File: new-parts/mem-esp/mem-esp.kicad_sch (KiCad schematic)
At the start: 63 parts, among them J1 Conn_02x02_Odd_Even, J2 BHR-10-VUA, J3 BHR-10-VUA, J4 Conn_02x01, J5 Conn_02x01, J6 Conn_02x01, J7 Conn_02x01, U1 MC78M06_TO252, U2 ESP32-S3-DevKitC, U3 LTV-247, U4 LTV-247, U5 DRV8908, U6 LTV-247, U7 LTV-247, U8 LTV-247

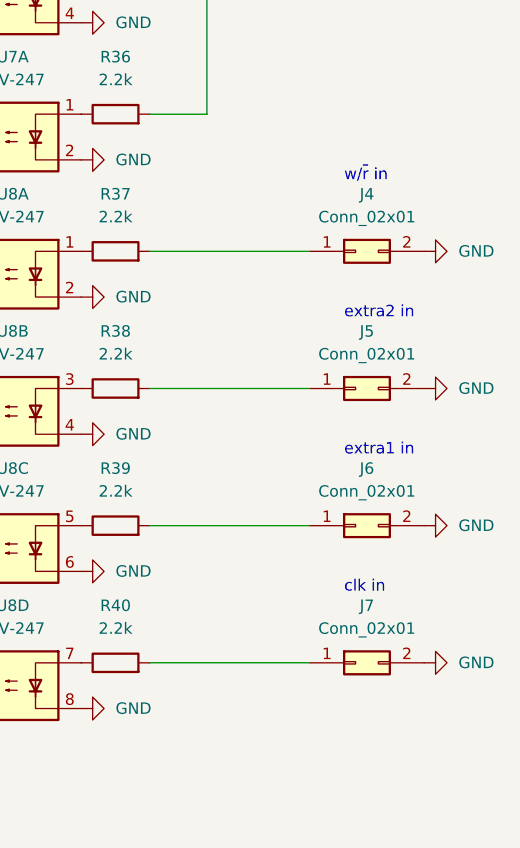
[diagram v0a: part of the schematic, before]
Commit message: Change all two-pin headers for control + ground to control only.
This is to prevent accidental short circuits when they are plugged in the
wrong way.
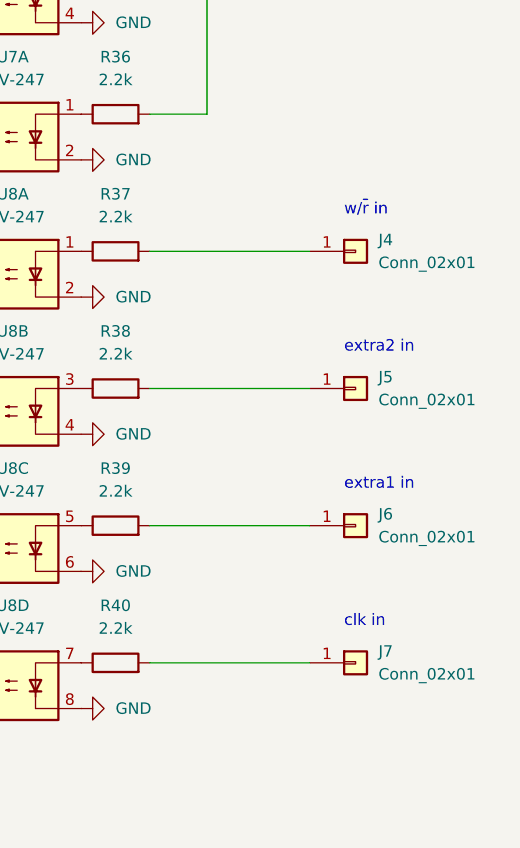
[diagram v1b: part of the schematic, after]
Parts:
- J4, J5, J6, J7: footprint Connector_PinHeader_2.54mm:PinHeader_1x02_P2.54mm_Vertical -> Connector_PinHeader_2.54mm:PinHeader_1x01_P2.54mm_Vertical; symbol Connector_Generic:Conn_02x01 -> Connector_Generic:Conn_01x01
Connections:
- net GND: no longer J4.2 (Pin_2), J5.2 (Pin_2), J6.2 (Pin_2), J7.2 (Pin_2)
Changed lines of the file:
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@@
     (effects (font (size 1.27 1.27)) (justify left top))
   )
-  (text "clk in" (at 386.08 182.88 0)
+  (text "clk in" (at 386.08 186.69 0)
     (effects (font (size 1.27 1.27)) (justify left bottom))
   )
-  (text "w/~{r} in" (at 386.08 137.16 0)
+  (text "w/~{r} in" (at 386.08 140.97 0)
     (effects (font (size 1.27 1.27)) (justify left bottom))
   )
@@
     (effects (font (size 1.27 1.27)) (justify left bottom))
   )
-  (text "extra2 in" (at 386.08 152.4 0)
+  (text "extra2 in" (at 386.08 156.21 0)
     (effects (font (size 1.27 1.27)) (justify left bottom))
   )
-  (text "extra1 in" (at 386.08 167.64 0)
+  (text "extra1 in" (at 386.08 171.45 0)
     (effects (font (size 1.27 1.27)) (justify left bottom))
   )
@@
     )
   )
-  (symbol (lib_id "Connector_Generic:Conn_02x01") (at 387.35 160.02 0) (unit 1)
+  (symbol (lib_id "Connector_Generic:Conn_01x01") (at 387.35 160.02 0) (unit 1)
     (in_bom yes) (on_board yes) (dnp no) (fields_autoplaced)
-    (property "Reference" "J5" (at 388.62 153.67 0)
-      (effects (font (size 1.27 1.27)))
+    (property "Reference" "J5" (at 389.89 158.75 0)
+      (effects (font (size 1.27 1.27)) (justify left))
     )
-    (property "Value" "Conn_02x01" (at 388.62 156.21 0)
-      (effects (font (size 1.27 1.27)))
+    (property "Value" "Conn_02x01" (at 389.89 161.29 0)
+      (effects (font (size 1.27 1.27)) (justify left))
     )
-    (property "Footprint" "Connector_PinHeader_2.54mm:PinHeader_1x02_P2.54mm_Vertical" (at 387.35 160.02 0)
+    (property "Footprint" "Connector_PinHeader_2.54mm:PinHeader_1x01_P2.54mm_Vertical" (at 387.35 160.02 0)
       (effects (font (size 1.27 1.27)) hide)
     )
@@
     )
     (pin "1")
-    (pin "2")
     (instances
       (project "mem-esp"
@@
     )
   )
-  (symbol (lib_id "Connector_Generic:Conn_02x01") (at 387.35 190.5 0) (unit 1)
+  (symbol (lib_id "Connector_Generic:Conn_01x01") (at 387.35 190.5 0) (unit 1)
     (in_bom yes) (on_board yes) (dnp no) (fields_autoplaced)
-    (property "Reference" "J7" (at 388.62 184.15 0)
-      (effects (font (size 1.27 1.27)))
+    (property "Reference" "J7" (at 389.89 189.23 0)
+      (effects (font (size 1.27 1.27)) (justify left))
     )
-    (property "Value" "Conn_02x01" (at 388.62 186.69 0)
-      (effects (font (size 1.27 1.27)))
+    (property "Value" "Conn_02x01" (at 389.89 191.77 0)
+      (effects (font (size 1.27 1.27)) (justify left))
     )
-    (property "Footprint" "Connector_PinHeader_2.54mm:PinHeader_1x02_P2.54mm_Vertical" (at 387.35 190.5 0)
+    (property "Footprint" "Connector_PinHeader_2.54mm:PinHeader_1x01_P2.54mm_Vertical" (at 387.35 190.5 0)
       (effects (font (size 1.27 1.27)) hide)
     )
@@
     )
     (pin "1")
-    (pin "2")
     (instances
       (project "mem-esp"
@@
     )
   )
-  (symbol (lib_id "power:GND") (at 394.97 175.26 90) (unit 1)
-    (in_bom yes) (on_board yes) (dnp no) (fields_autoplaced)
-    (property "Reference" "#PWR094" (at 401.32 175.26 0)
-      (effects (font (size 1.27 1.27)) hide)
-    )
-    (property "Value" "GND" (at 398.78 175.26 90)
-      (effects (font (size 1.27 1.27)) (justify right))
-    )
-    (property "Footprint" "" (at 394.97 175.26 0)
-      (effects (font (size 1.27 1.27)) hide)
-    )
-    (property "Datasheet" "" (at 394.97 175.26 0)
-      (effects (font (size 1.27 1.27)) hide)
-    )
-    (pin "1")
-    (instances
-      (project "mem-esp"
-        (path "/8e7358e7-c3ef-4f3e-9154-e7eba01c544e"
-          (reference "#PWR094") (unit 1)
-        )
-      )
-    )
-  )
   (symbol (lib_id "power:+3V3") (at 231.14 99.06 90) (unit 1)
     (in_bom yes) (on_board yes) (dnp no) (fields_autoplaced)
@@
     )
   )
-  (symbol (lib_id "power:GND") (at 394.97 144.78 90) (unit 1)
-    (in_bom yes) (on_board yes) (dnp no) (fields_autoplaced)
-    (property "Reference" "#PWR093" (at 401.32 144.78 0)
-      (effects (font (size 1.27 1.27)) hide)
-    )
-    (property "Value" "GND" (at 398.78 144.78 90)
-      (effects (font (size 1.27 1.27)) (justify right))
-    )
-    (property "Footprint" "" (at 394.97 144.78 0)
-      (effects (font (size 1.27 1.27)) hide)
-    )
-    (property "Datasheet" "" (at 394.97 144.78 0)
-      (effects (font (size 1.27 1.27)) hide)
-    )
-    (pin "1")
-    (instances
-      (project "mem-esp"
-        (path "/8e7358e7-c3ef-4f3e-9154-e7eba01c544e"
-          (reference "#PWR093") (unit 1)
-        )
-      )
-    )
-  )
   (symbol (lib_id "Isolator:LTV-247") (at 349.25 101.6 0) (mirror y) (unit 3)
     (in_bom yes) (on_board yes) (dnp no) (fields_autoplaced)
@@
     )
   )
-  (symbol (lib_id "Connector_Generic:Conn_02x01") (at 387.35 144.78 0) (unit 1)
+  (symbol (lib_id "Connector_Generic:Conn_01x01") (at 387.35 144.78 0) (unit 1)
     (in_bom yes) (on_board yes) (dnp no) (fields_autoplaced)
-    (property "Reference" "J4" (at 388.62 138.43 0)
-      (effects (font (size 1.27 1.27)))
+    (property "Reference" "J4" (at 389.89 143.51 0)
+      (effects (font (size 1.27 1.27)) (justify left))
     )
-    (property "Value" "Conn_02x01" (at 388.62 140.97 0)
-      (effects (font (size 1.27 1.27)))
+    (property "Value" "Conn_02x01" (at 389.89 146.05 0)
+      (effects (font (size 1.27 1.27)) (justify left))
     )
-    (property "Footprint" "Connector_PinHeader_2.54mm:PinHeader_1x02_P2.54mm_Vertical" (at 387.35 144.78 0)
+    (property "Footprint" "Connector_PinHeader_2.54mm:PinHeader_1x01_P2.54mm_Vertical" (at 387.35 144.78 0)
       (effects (font (size 1.27 1.27)) hide)
     )
@@
     )
     (pin "1")
-    (pin "2")
     (instances
       (project "mem-esp"
@@
     )
   )
-  (symbol (lib_id "power:GND") (at 394.97 160.02 90) (unit 1)
-    (in_bom yes) (on_board yes) (dnp no) (fields_autoplaced)
-    (property "Reference" "#PWR095" (at 401.32 160.02 0)
-      (effects (font (size 1.27 1.27)) hide)
-    )
-    (property "Value" "GND" (at 398.78 160.02 90)
-      (effects (font (size 1.27 1.27)) (justify right))
-    )
-    (property "Footprint" "" (at 394.97 160.02 0)
-      (effects (font (size 1.27 1.27)) hide)
-    )
-    (property "Datasheet" "" (at 394.97 160.02 0)
-      (effects (font (size 1.27 1.27)) hide)
-    )
-    (pin "1")
-    (instances
-      (project "mem-esp"
-        (path "/8e7358e7-c3ef-4f3e-9154-e7eba01c544e"
-          (reference "#PWR095") (unit 1)
-        )
-      )
-    )
-  )
   (symbol (lib_id "power:+3V3") (at 231.14 68.58 90) (unit 1)
     (in_bom yes) (on_board yes) (dnp no) (fields_autoplaced)
@@
     )
   )
-  (symbol (lib_id "Connector_Generic:Conn_02x01") (at 387.35 175.26 0) (unit 1)
+  (symbol (lib_id "Connector_Generic:Conn_01x01") (at 387.35 175.26 0) (unit 1)
     (in_bom yes) (on_board yes) (dnp no) (fields_autoplaced)
-    (property "Reference" "J6" (at 388.62 168.91 0)
-      (effects (font (size 1.27 1.27)))
+    (property "Reference" "J6" (at 389.89 173.99 0)
+      (effects (font (size 1.27 1.27)) (justify left))
     )
-    (property "Value" "Conn_02x01" (at 388.62 171.45 0)
-      (effects (font (size 1.27 1.27)))
+    (property "Value" "Conn_02x01" (at 389.89 176.53 0)
+      (effects (font (size 1.27 1.27)) (justify left))
     )
-    (property "Footprint" "Connector_PinHeader_2.54mm:PinHeader_1x02_P2.54mm_Vertical" (at 387.35 175.26 0)
+    (property "Footprint" "Connector_PinHeader_2.54mm:PinHeader_1x01_P2.54mm_Vertical" (at 387.35 175.26 0)
       (effects (font (size 1.27 1.27)) hide)
     )
@@
     )
     (pin "1")
-    (pin "2")
     (instances
       (project "mem-esp"
@@
         )
       )
-    )
-  )
-  (symbol (lib_id "power:GND") (at 394.97 190.5 90) (unit 1)
-    (in_bom yes) (on_board yes) (dnp no) (fields_autoplaced)
-    (property "Reference" "#PWR092" (at 401.32 190.5 0)
-      (effects (font (size 1.27 1.27)) hide)
-    )
-    (property "Value" "GND" (at 398.78 190.5 90)
-      (effects (font (size 1.27 1.27)) (justify right))
-    )
-    (property "Footprint" "" (at 394.97 190.5 0)
-      (effects (font (size 1.27 1.27)) hide)
-    )
-    (property "Datasheet" "" (at 394.97 190.5 0)
-      (effects (font (size 1.27 1.27)) hide)
-    )
-    (pin "1")
-    (instances
-      (project "mem-esp"
-        (path "/8e7358e7-c3ef-4f3e-9154-e7eba01c544e"
-          (reference "#PWR092") (unit 1)
-        )
-      )

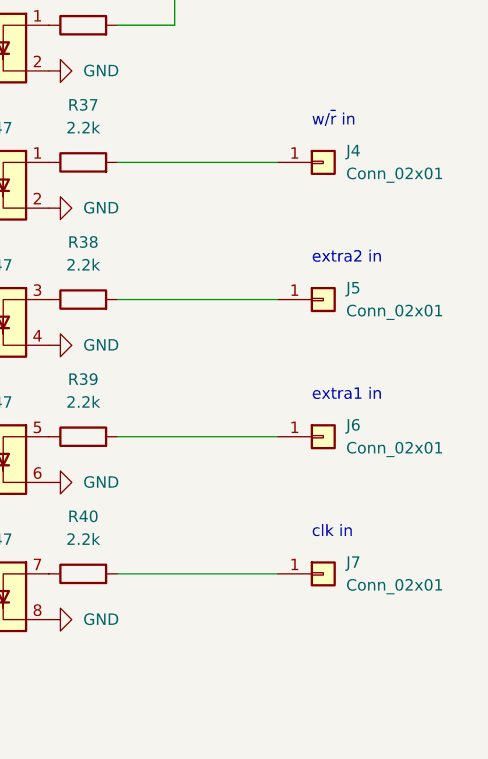
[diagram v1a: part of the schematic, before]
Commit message: Fix connector values: change names from 2 rows to 1 row.
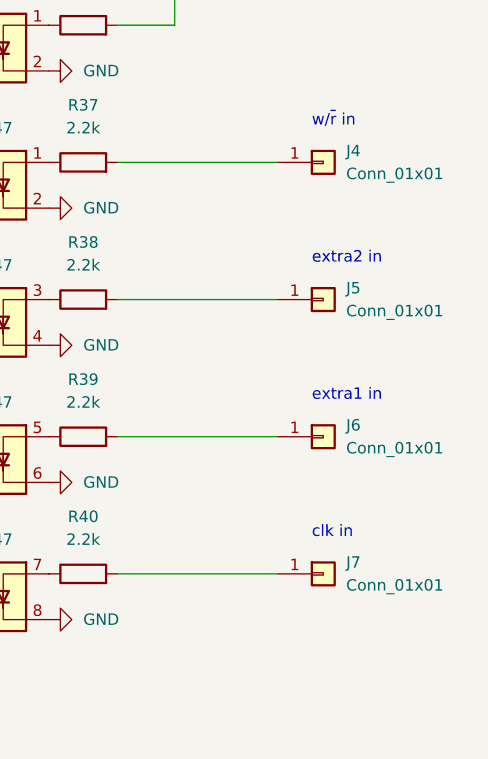
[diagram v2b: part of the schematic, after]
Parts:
- J4, J5, J6, J7: value Conn_02x01 -> Conn_01x01
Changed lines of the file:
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@@
       (effects (font (size 1.27 1.27)) (justify left))
     )
-    (property "Value" "Conn_02x01" (at 389.89 161.29 0)
+    (property "Value" "Conn_01x01" (at 389.89 161.29 0)
       (effects (font (size 1.27 1.27)) (justify left))
     )
@@
       (effects (font (size 1.27 1.27)) (justify left))
     )
-    (property "Value" "Conn_02x01" (at 389.89 191.77 0)
+    (property "Value" "Conn_01x01" (at 389.89 191.77 0)
       (effects (font (size 1.27 1.27)) (justify left))
     )
@@
       (effects (font (size 1.27 1.27)) (justify left))
     )
-    (property "Value" "Conn_02x01" (at 389.89 146.05 0)
+    (property "Value" "Conn_01x01" (at 389.89 146.05 0)
       (effects (font (size 1.27 1.27)) (justify left))
     )
@@
       (effects (font (size 1.27 1.27)) (justify left))
     )
-    (property "Value" "Conn_02x01" (at 389.89 176.53 0)
-      (effects (font (size 1.27 1.27)) (justify left))
-    )
+    (property "Value" "Conn_01x01" (at 389.89 176.53 0)
+      (effects (font (size 1.27 1.27)) (justify left))
+    )

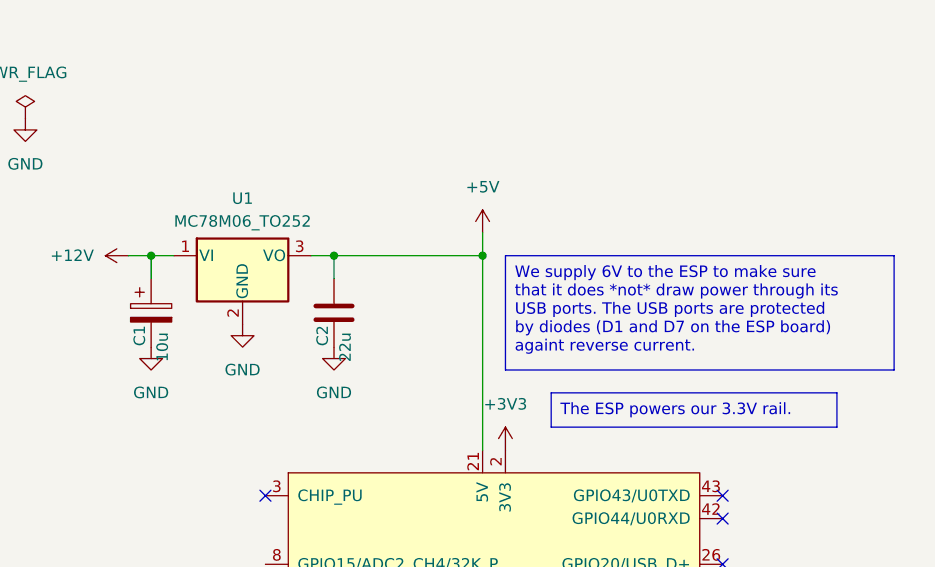
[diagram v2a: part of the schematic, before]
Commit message: mem-esp: Change to a THT power regulator for better heat dissipation.
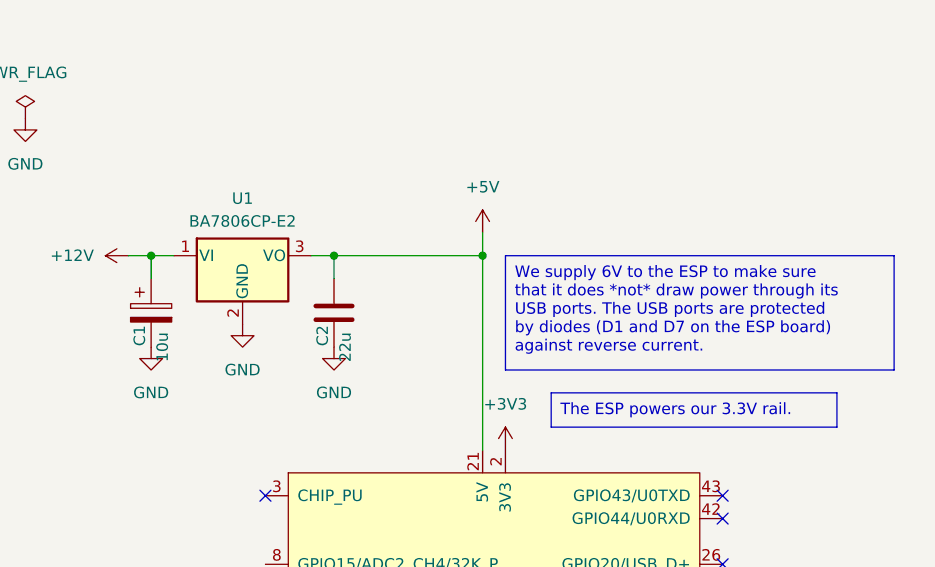
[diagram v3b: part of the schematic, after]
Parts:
- removed U1: MC78M06_TO252, Package_TO_SOT_SMD:TO-252-2, symbol Regulator_Linear:MC78M05_TO252
- added U1: BA7806CP-E2, Package_TO_SOT_THT:TO-220-3_Vertical, symbol Regulator_Linear:LM7806_TO220
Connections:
- net +12V: now also U1.1 (VI)
- net +5V: now also U1.3 (VO)
- net GND: now also U1.2 (GND)
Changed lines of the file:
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@@
     (effects (font (size 1.27 1.27)) (justify left))
   )
-  (text_box "We supply 6V to the ESP to make sure that it does *not* draw power through its USB ports. The USB ports are protected by diodes (D1 and D7 on the ESP board) againt reverse current."
+  (text_box "We supply 6V to the ESP to make sure that it does *not* draw power through its USB ports. The USB ports are protected by diodes (D1 and D7 on the ESP board) against reverse current."
     (at 142.24 36.83 0) (size 43.18 12.7)
     (stroke (width 0) (type default))
@@
     )
   )
+  (symbol (lib_id "Regulator_Linear:LM7806_TO220") (at 113.03 36.83 0) (unit 1)
+    (in_bom yes) (on_board yes) (dnp no) (fields_autoplaced)
+    (property "Reference" "U1" (at 113.03 30.48 0)
+      (effects (font (size 1.27 1.27)))
+    )
+    (property "Value" "BA7806CP-E2" (at 113.03 33.02 0)
+      (effects (font (size 1.27 1.27)))
+    )
+    (property "Footprint" "Package_TO_SOT_THT:TO-220-3_Vertical" (at 113.03 31.115 0)
+      (effects (font (size 1.27 1.27) italic) hide)
+    )
+    (property "Datasheet" "https://www.onsemi.cn/PowerSolutions/document/MC7800-D.PDF" (at 113.03 38.1 0)
+      (effects (font (size 1.27 1.27)) hide)
+    )
+    (pin "1")
+    (pin "3")
+    (pin "2")
+    (instances
+      (project "mem-esp"
+        (path "/8e7358e7-c3ef-4f3e-9154-e7eba01c544e"
+          (reference "U1") (unit 1)
+        )
+      )
+    )
+  )
   (symbol (lib_id "power:+3V3") (at 341.63 160.02 90) (unit 1)
     (in_bom yes) (on_board yes) (dnp no) (fields_autoplaced)
@@
         )
       )
-    )
-  )
-  (symbol (lib_id "Regulator_Linear:MC78M05_TO252") (at 113.03 36.83 0) (unit 1)
-    (in_bom yes) (on_board yes) (dnp no) (fields_autoplaced)
-    (property "Reference" "U1" (at 113.03 30.48 0)
-      (effects (font (size 1.27 1.27)))
-    )
-    (property "Value" "MC78M06_TO252" (at 113.03 33.02 0)
-      (effects (font (size 1.27 1.27)))
-    )
-    (property "Footprint" "Package_TO_SOT_SMD:TO-252-2" (at 113.03 31.115 0)
-      (effects (font (size 1.27 1.27) italic) hide)
-    )
-    (property "Datasheet" "https://www.onsemi.com/pub/Collateral/MC78M00-D.PDF" (at 113.03 38.1 0)
-      (effects (font (size 1.27 1.27)) hide)
-    )
-    (pin "3")
-    (pin "1")
-    (pin "2")
-    (instances
-      (project "mem-esp"
-        (path "/8e7358e7-c3ef-4f3e-9154-e7eba01c544e"
-          (reference "U1") (unit 1)
-        )
-      )

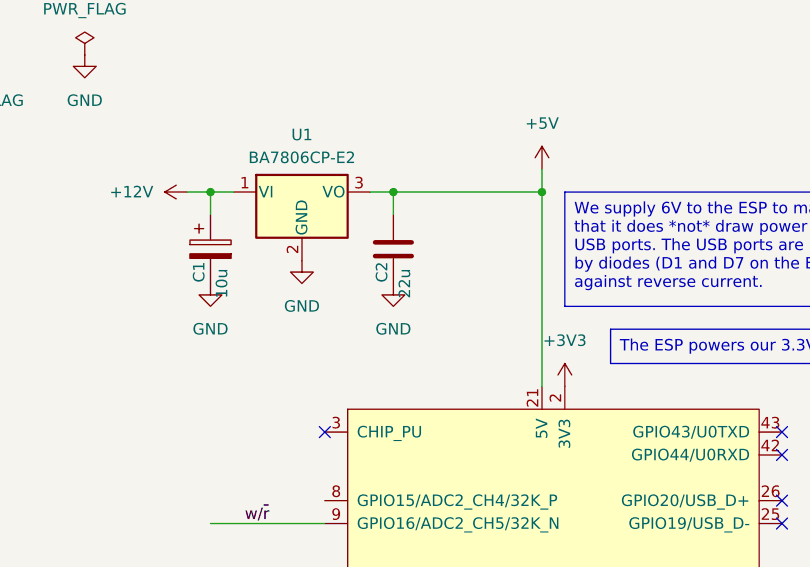
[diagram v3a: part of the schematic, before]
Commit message: mem-esp: Change capacitor behind LDO to a simpler part.
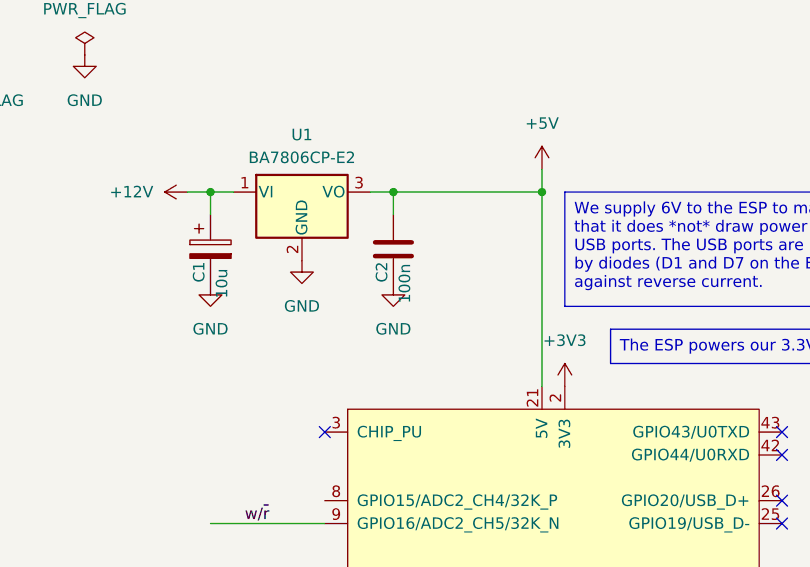
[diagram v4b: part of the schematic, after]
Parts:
- C2: value 22u -> 100n
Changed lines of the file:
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@@
       (effects (font (size 1.27 1.27)))
     )
-    (property "Value" "22u" (at 124.46 46.99 90)
+    (property "Value" "100n" (at 124.46 46.99 90)
       (effects (font (size 1.27 1.27)))
     )
